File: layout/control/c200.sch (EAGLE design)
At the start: 65 parts, among them IC1 STM32F103C8T, IC2 LP2985-SOT23-5, IC3 IC_USBLC6-2, IC4 IC_USBLC6-2, IC5 LT1619ES8, IC6 LP2985-SOT23-5, IC7 IRF7470, T1 LPISR, X1 MINI-USB-SCHIELD-32005-201, Y1 532-CRYSTAL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

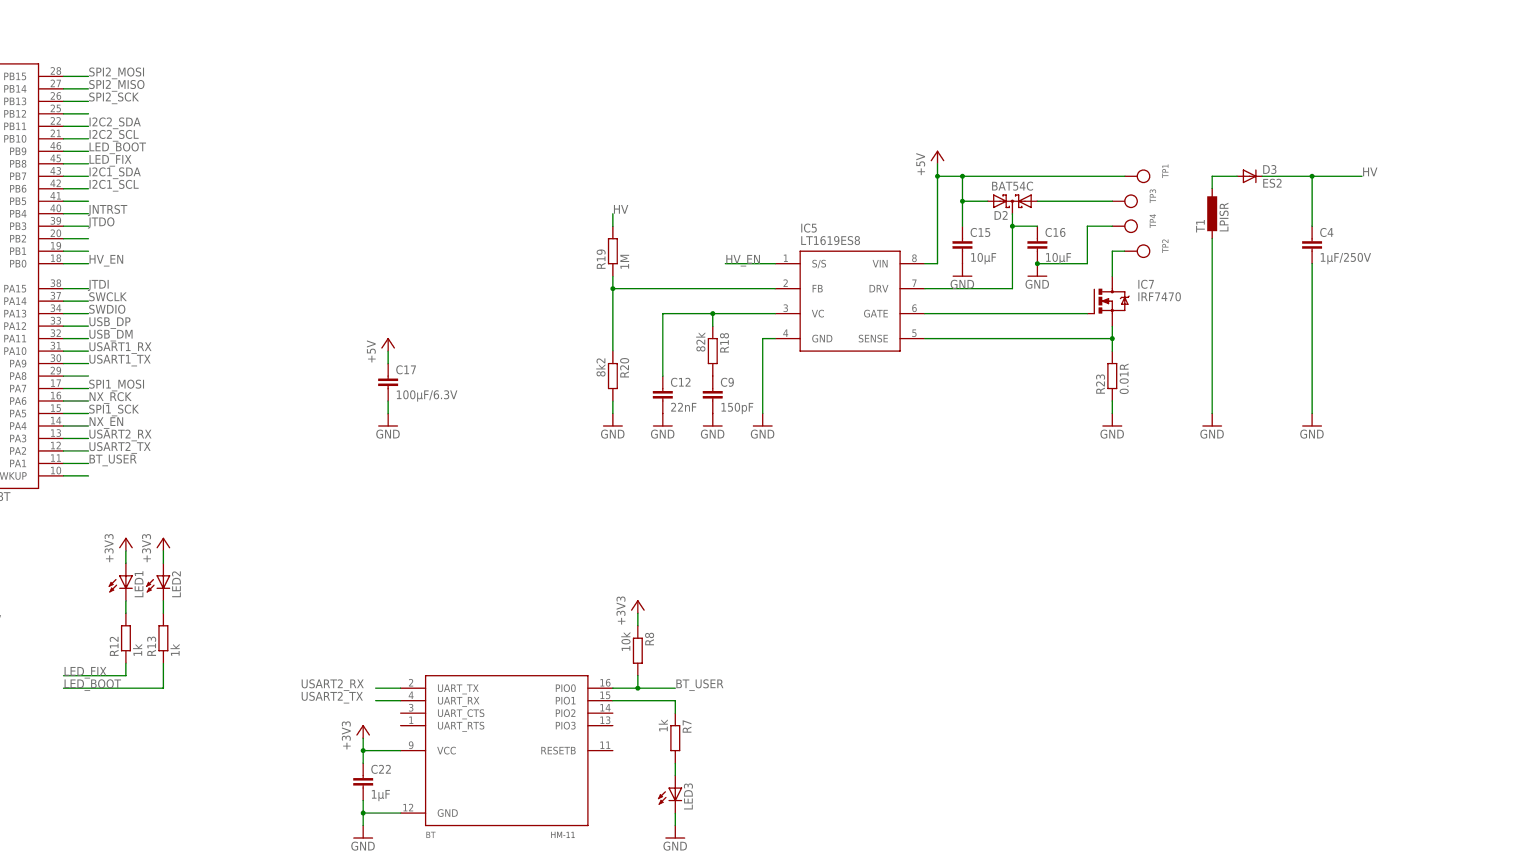
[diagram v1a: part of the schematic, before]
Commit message: Added ESP-12
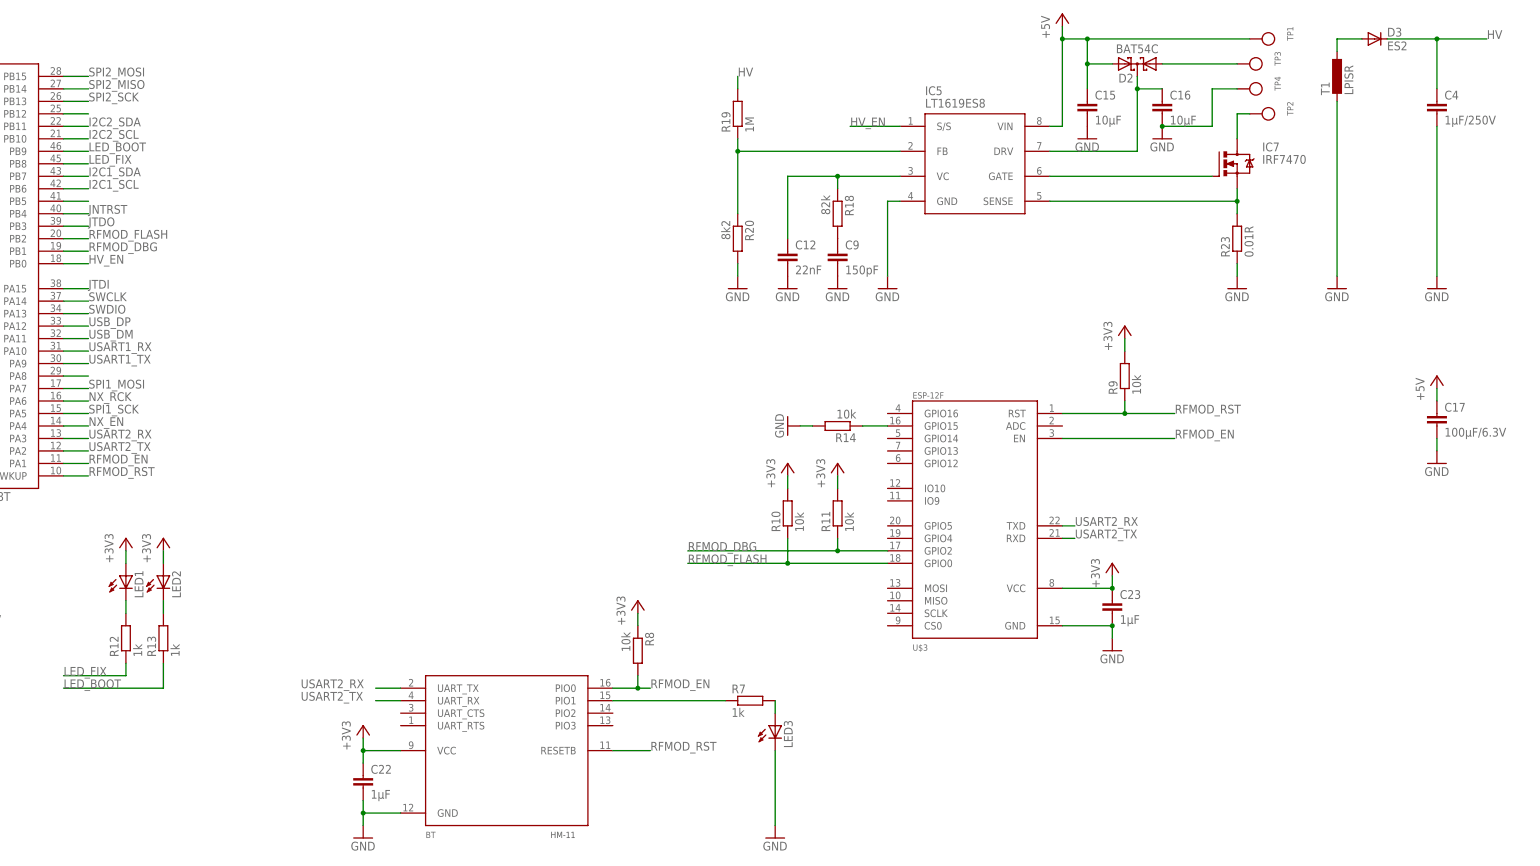
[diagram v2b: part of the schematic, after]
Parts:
- added C23: 1µF, rcl:C-EUC0603
- added R10, R11, R14, R9: 10k, rcl:R-EU_R0603
- added U$3: ESP-12F, espressif:ESP-12F
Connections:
- removed net BT_USER: BT.PIO0, IC1MCU.PA1, R8.2
- removed net N$32: IC1MCU.PB1
- removed net N$34: IC1MCU.PB2
- removed net N$42: IC1MCU.PA0-WKUP
- new net N$6: R14.1, U$3.GPIO15
- new net RFMOD_DBG: IC1MCU.PB1, R11.1, U$3.GPIO2
- new net RFMOD_EN: BT.PIO0, IC1MCU.PA1, R8.2, U$3.EN
- new net RFMOD_FLASH: IC1MCU.PB2, R10.1, U$3.GPIO0
- new net RFMOD_RST: BT.RESETB, IC1MCU.PA0-WKUP, R9.1, U$3.RST
- net +3V3: now also C23.1, R10.2, R11.2, R9.2, U$3.VCC
- net GND: now also C23.2, R14.2, U$3.GND
- net USART2_RX: now also U$3.TXD
- net USART2_TX: now also U$3.RXD
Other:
- moved on the sheet: C12, C15, C16, C17, C4, C9, D2, D3, IC5, IC7, LED3, R18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
